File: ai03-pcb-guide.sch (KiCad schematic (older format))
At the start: 24 parts, among them SW1 SW_Push, U1 ATmega32U4-AU, Y1 Crystal_GND24_Small

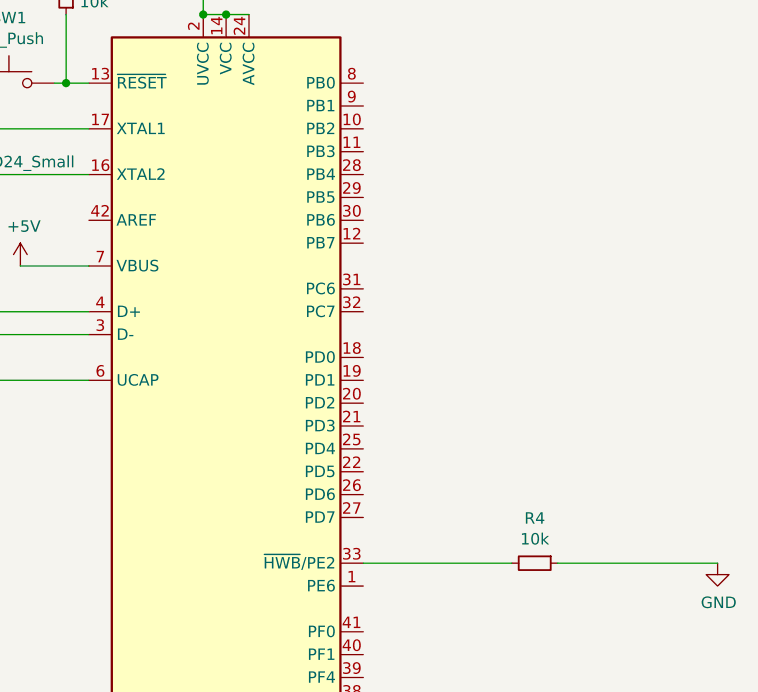
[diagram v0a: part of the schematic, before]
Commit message: components placed
components placed in their place and routed correctly.
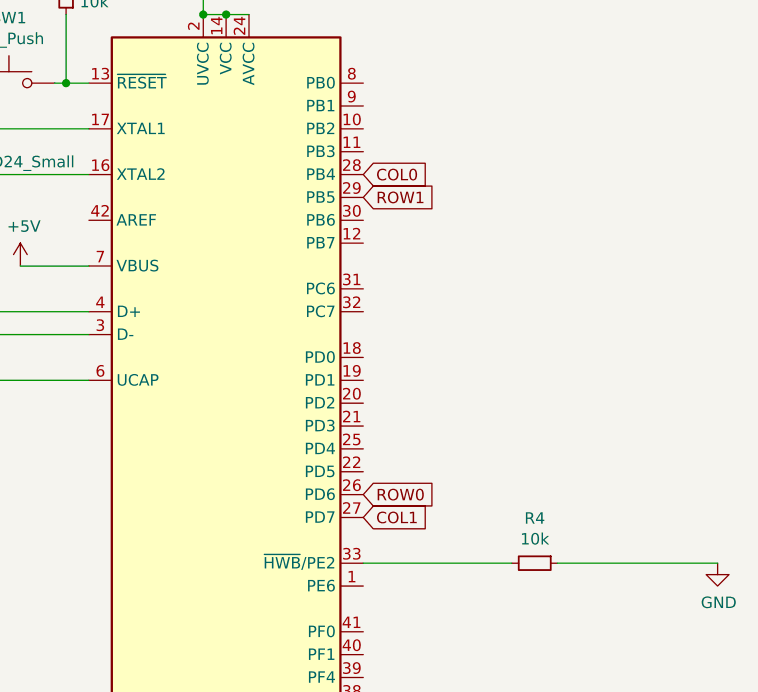
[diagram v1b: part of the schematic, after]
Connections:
- net COL0: now also U1.28 (PB4)
- net COL1: now also U1.27 (PD7)
- net ROW0: now also U1.26 (PD6)
- net ROW1: now also U1.29 (PB5)
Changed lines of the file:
@@
 EESchema Schematic File Version 4
+LIBS:ai03-pcb-guide-cache
 EELAYER 30 0
 EELAYER END
@@
 Text GLabel 900  5300 0    50   Input ~ 0
 ROW1
+Text GLabel 9500 4450 2    50   Input ~ 0
+COL1
+Text GLabel 9500 2950 2    50   Input ~ 0
+COL0
+Text GLabel 9500 3050 2    50   Input ~ 0
+ROW1
+Text GLabel 9500 4350 2    50   Input ~ 0
+ROW0
 $EndSCHEMATC
